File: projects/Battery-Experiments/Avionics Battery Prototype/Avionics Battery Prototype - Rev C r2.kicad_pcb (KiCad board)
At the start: 2 copper layers, 132.1 x 121.9 mm, 60 parts, among them J1 Jack-DC, J2 Enable, J3 UART, J4 SBW JTAG, U1 OPA4197, U2 OPA4197, U3 CD4052B, U4 LT1763, U5 MSP430G2233, U6 CD40109B

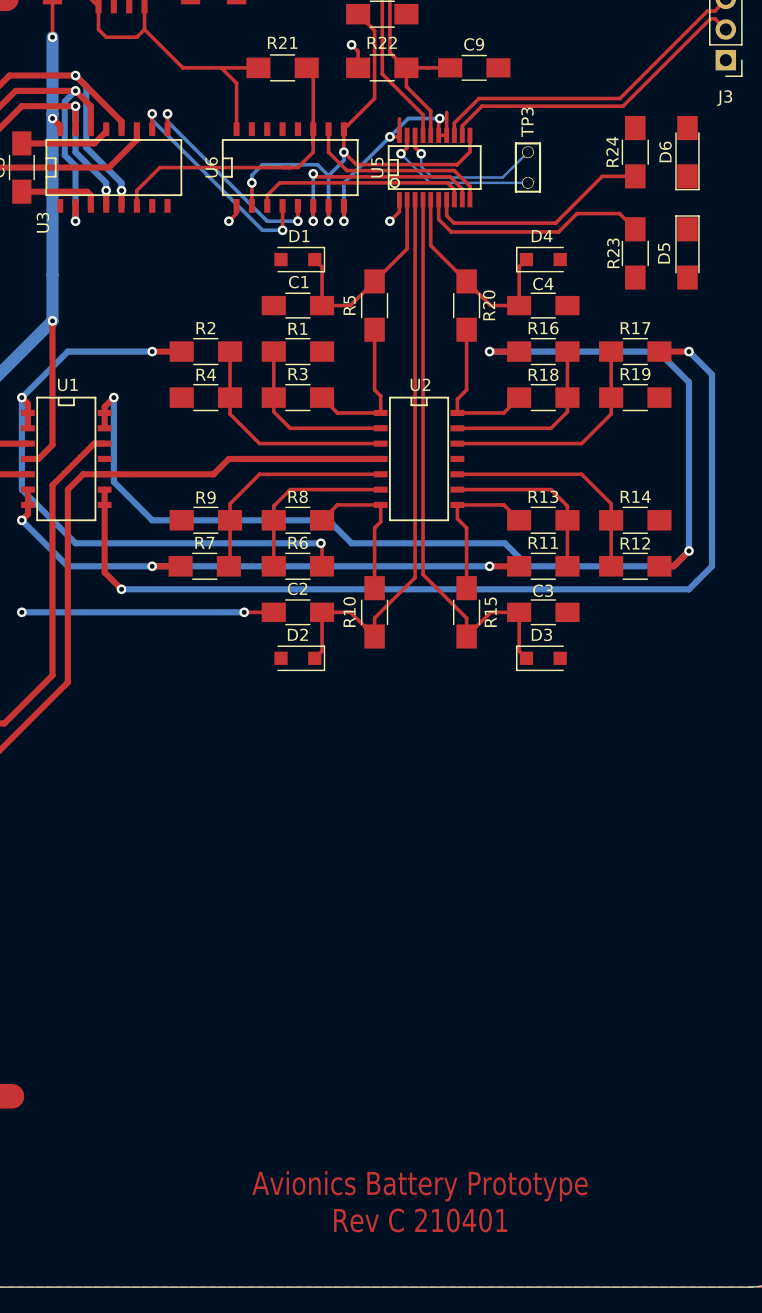
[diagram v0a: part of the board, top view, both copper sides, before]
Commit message: AVB Rev C and XTAL Plug Final
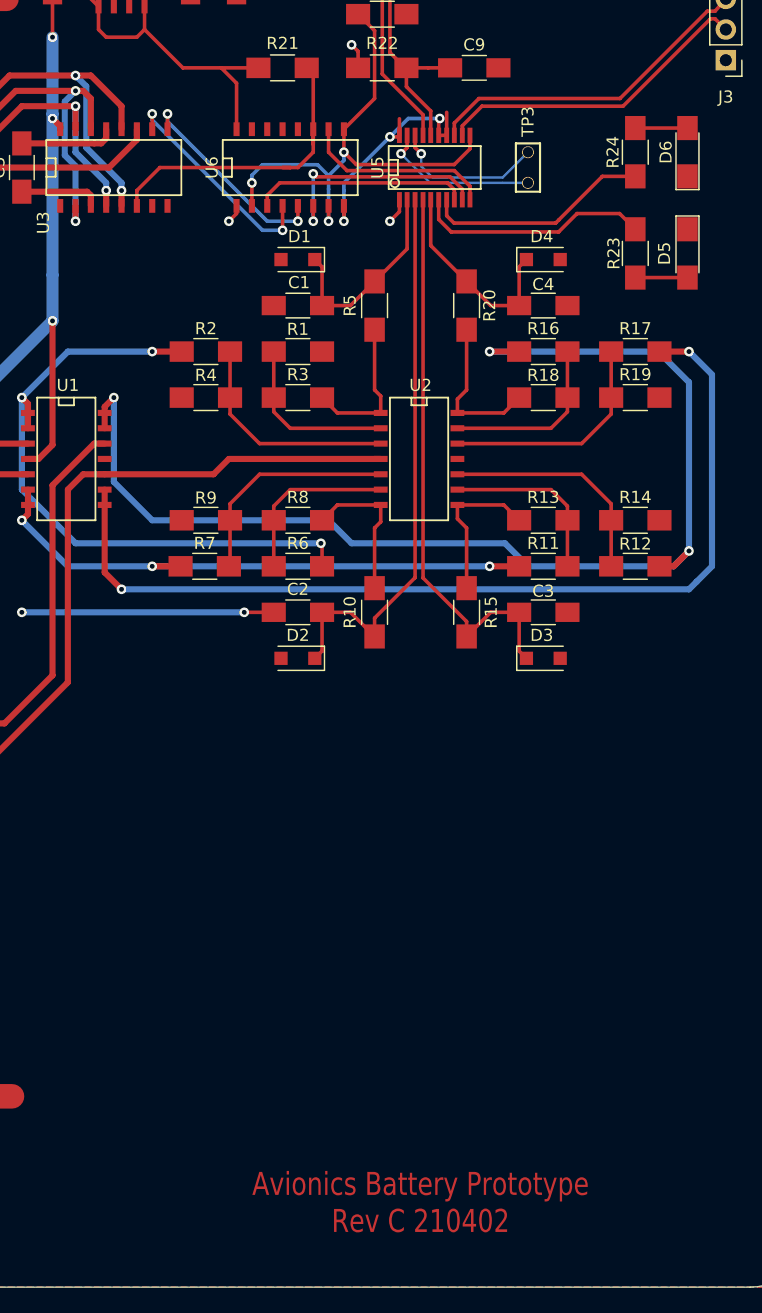
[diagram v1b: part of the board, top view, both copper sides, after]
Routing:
- net Net-(D6-Pad2): track 0.00 -> 4.32 mm
- net Net-(D5-Pad2): track 0.00 -> 4.32 mm
- net Net-(BT1-Pad1): track 153.5 -> 154.2 mm
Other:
- board text added: "Avionics Battery Prototype Rev C 210402"
- board text removed: "Avionics Battery Prototype Rev C 210401"
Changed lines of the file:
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@@
     (thickness 1.6)
     (drawings 22)
-    (tracks 440)
+    (tracks 443)
     (zones 0)
     (modules 60)
@@
   (title_block
     (title "Avionics Battery Prototype")
-    (date 2021-04-01)
+    (date 2021-04-02)
     (rev B)
     (company K7ARX)
@@
   )
   (setup
-    (last_trace_width 2.032)
+    (last_trace_width 0.508)
     (user_trace_width 0.508)
     (user_trace_width 1.016)
@@
   )
   (gr_line (start 43.815 27.94) (end 165.735 27.94) (layer Edge.Cuts) (width 0.05))
-  (gr_text "Avionics Battery Prototype \nRev C 210401" (at 138.43 142.875) (layer F.Cu)
+  (gr_text "Avionics Battery Prototype \nRev C 210402" (at 138.43 142.875) (layer F.Cu)
     (effects (font (size 1.905 1.524) (thickness 0.254)))
   )
@@
   (via (at 97.79 53.34) (size 0.8) (drill 0.4) (layers F.Cu B.Cu) (net 1))
   (via (at 109.855 49.53) (size 0.8) (drill 0.4) (layers F.Cu B.Cu) (net 1))
-  (segment (start 113.665 53.34) (end 109.855 49.53) (width 0.508) (layer F.Cu) (net 1))
-  (segment (start 113.665 53.975) (end 113.665 53.34) (width 0.508) (layer F.Cu) (net 1))
   (segment (start 113.665 58.42) (end 110.744 55.499) (width 0.508) (layer B.Cu) (net 1))
   (segment (start 110.744 50.419) (end 109.855 49.53) (width 0.508) (layer B.Cu) (net 1))
@@
   (segment (start 80.68 63.18) (end 88.045 63.18) (width 2.032) (layer F.Cu) (net 1))
   (segment (start 60.68 43.18) (end 80.68 63.18) (width 2.032) (layer F.Cu) (net 1))
+  (segment (start 111.125 49.53) (end 109.855 49.53) (width 0.508) (layer F.Cu) (net 1))
+  (segment (start 113.665 53.975) (end 113.665 52.07) (width 0.508) (layer F.Cu) (net 1))
+  (segment (start 113.665 52.07) (end 111.125 49.53) (width 0.508) (layer F.Cu) (net 1))
   (segment (start 88.045 43.18) (end 104.14 43.18) (width 2.032) (layer F.Cu) (net 2))
   (segment (start 139.9286 54.483) (end 140.589 54.483) (width 0.3) (layer F.Cu) (net 2))
@@
   (via (at 109.855 50.8) (size 0.8) (drill 0.4) (layers F.Cu B.Cu) (net 3))
   (segment (start 109.855 50.959998) (end 109.855 50.8) (width 0.3) (layer F.Cu) (net 3))
-  (segment (start 111.125 53.975) (end 111.125 52.229998) (width 0.508) (layer F.Cu) (net 3))
   (segment (start 109.855 57.023) (end 109.855 61.595) (width 0.508) (layer B.Cu) (net 3))
   (segment (start 108.966 56.134) (end 109.855 57.023) (width 0.508) (layer B.Cu) (net 3))
@@
   (segment (start 104.902 50.8) (end 101.092 54.61) (width 0.508) (layer F.Cu) (net 3))
   (segment (start 109.855 50.8) (end 104.902 50.8) (width 0.508) (layer F.Cu) (net 3))
-  (segment (start 111.125 52.07) (end 111.125 52.229998) (width 0.508) (layer F.Cu) (net 3))
-  (segment (start 109.855 50.8) (end 111.125 52.07) (width 0.508) (layer F.Cu) (net 3))
   (segment (start 58.955 54.61) (end 50.385 63.18) (width 0.508) (layer B.Cu) (net 3))
   (segment (start 97.79 54.61) (end 58.955 54.61) (width 0.508) (layer B.Cu) (net 3))
@@
   (segment (start 80.68 83.18) (end 88.045 83.18) (width 2.032) (layer F.Cu) (net 3))
   (segment (start 60.68 63.18) (end 80.68 83.18) (width 2.032) (layer F.Cu) (net 3))
+  (segment (start 111.125 53.975) (end 111.125 51.435) (width 0.508) (layer F.Cu) (net 3))
+  (segment (start 110.49 50.8) (end 109.855 50.8) (width 0.508) (layer F.Cu) (net 3))
+  (segment (start 111.125 51.435) (end 110.49 50.8) (width 0.508) (layer F.Cu) (net 3))
   (segment (start 111.3965 80.01) (end 112.268 80.01) (width 0.508) (layer F.Cu) (net 4))
   (segment (start 107.95 83.4565) (end 111.3965 80.01) (width 0.508) (layer F.Cu) (net 4))
@@
   (segment (start 146.59 97.19) (end 147.19 97.79) (width 0.3) (layer F.Cu) (net 8))
   (segment (start 146.59 93.98) (end 146.59 97.19) (width 0.3) (layer F.Cu) (net 8))
-  (segment (start 142.24 94.460002) (end 142.24 95.98) (width 0.3) (layer F.Cu) (net 8))
-  (segment (start 138.6332 90.853202) (end 142.24 94.460002) (width 0.3) (layer F.Cu) (net 8))
-  (segment (start 138.6332 59.817) (end 138.6332 90.853202) (width 0.3) (layer F.Cu) (net 8))
+  (segment (start 142.24 94.742) (end 142.24 95.98) (width 0.3) (layer F.Cu) (net 8))
+  (segment (start 138.6332 91.1352) (end 142.24 94.742) (width 0.3) (layer F.Cu) (net 8))
+  (segment (start 138.6332 59.817) (end 138.6332 91.1352) (width 0.3) (layer F.Cu) (net 8))
   (segment (start 144.24 68.58) (end 142.24 66.58) (width 0.3) (layer F.Cu) (net 9))
   (segment (start 146.59 68.58) (end 144.24 68.58) (width 0.3) (layer F.Cu) (net 9))
@@
   (segment (start 110.8215 59.15) (end 111.125 59.4535) (width 0.508) (layer F.Cu) (net 10))
   (segment (start 105.41 59.15) (end 110.8215 59.15) (width 0.508) (layer F.Cu) (net 10))
-  (segment (start 112.395 54.160502) (end 112.395 53.975) (width 0.508) (layer F.Cu) (net 11))
-  (segment (start 111.405502 55.15) (end 112.395 54.160502) (width 0.508) (layer F.Cu) (net 11))
   (segment (start 105.41 55.15) (end 111.405502 55.15) (width 0.508) (layer F.Cu) (net 11))
+  (segment (start 112.395 53.975) (end 112.395 54.737) (width 0.508) (layer F.Cu) (net 11))
+  (segment (start 111.982 55.15) (end 111.405502 55.15) (width 0.508) (layer F.Cu) (net 11))
+  (segment (start 112.395 54.737) (end 111.982 55.15) (width 0.508) (layer F.Cu) (net 11))
   (segment (start 110.585 42.64) (end 111.76 43.815) (width 0.3) (layer F.Cu) (net 12))
   (segment (start 107.95 42.64) (end 110.585 42.64) (width 0.3) (layer F.Cu) (net 12))
@@
   (segment (start 139.2682 52.4642) (end 137.255 50.451) (width 0.3) (layer F.Cu) (net 15))
   (segment (start 139.2682 54.483) (end 139.2682 52.4642) (width 0.3) (layer F.Cu) (net 15))
+  (segment (start 156.21 66.262) (end 160.528 66.262) (width 0.3) (layer F.Cu) (net 16))
+  (segment (start 156.21 53.88) (end 160.528 53.88) (width 0.3) (layer F.Cu) (net 17))
   (segment (start 162.814 44.20399) (end 163.703 43.18) (width 0.3) (layer F.Cu) (net 18))
   (segment (start 154.94 51.435) (end 162.17101 44.20399) (width 0.3) (layer F.Cu) (net 18))
@@
   (segment (start 125.325001 56.919999) (end 124.46 57.785) (width 0.3) (layer B.Cu) (net 40))
   (segment (start 124.46 58.42) (end 124.46 60.325) (width 0.3) (layer F.Cu) (net 40))
-  (segment (start 142.5194 54.483) (end 142.5194 55.8546) (width 0.3) (layer F.Cu) (net 40))
-  (segment (start 141.45056 56.92344) (end 141.43111 56.90399) (width 0.3) (layer F.Cu) (net 40))
-  (segment (start 142.5194 55.8546) (end 141.45056 56.92344) (width 0.3) (layer F.Cu) (net 40))
-  (segment (start 141.43111 56.90399) (end 133.10399 56.90399) (width 0.3) (layer F.Cu) (net 40))
   (segment (start 132.08 55.88) (end 132.08 53.975) (width 0.3) (layer F.Cu) (net 40))
-  (segment (start 133.10399 56.90399) (end 132.08 55.88) (width 0.3) (layer F.Cu) (net 40))
   (via (at 132.08 55.88) (size 0.8) (drill 0.4) (layers F.Cu B.Cu) (net 40))
   (segment (start 132.08 56.559998) (end 130.81 57.829998) (width 0.3) (layer B.Cu) (net 40))
@@
   (segment (start 134.62 51.435) (end 134.62 45.815) (width 0.3) (layer F.Cu) (net 40))
   (segment (start 132.08 53.975) (end 134.62 51.435) (width 0.3) (layer F.Cu) (net 40))
+  (segment (start 142.5194 55.6006) (end 142.5194 54.483) (width 0.3) (layer F.Cu) (net 40))
+  (segment (start 141.21601 56.90399) (end 142.5194 55.6006) (width 0.3) (layer F.Cu) (net 40))
+  (segment (start 133.10399 56.90399) (end 141.21601 56.90399) (width 0.3) (layer F.Cu) (net 40))
+  (segment (start 132.08 55.88) (end 133.10399 56.90399) (width 0.3) (layer F.Cu) (net 40))
   (via (at 127 62.345) (size 0.8) (drill 0.4) (layers F.Cu B.Cu) (net 41))
   (segment (start 127 60.325) (end 127 62.345) (width 0.3) (layer F.Cu) (net 41))
